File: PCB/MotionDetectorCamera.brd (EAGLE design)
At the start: 211.5 x 44.5 mm, 172 parts, among them J1 JUMPER-SOLDER, J12 JUMPER-AMPHENOL-10129380-9020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, J13 JUMPER-AMPHENOL-10129380-9020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, J14 JUMPER-AMPHENOL-10129380-9020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, J15 JUMPER-AMPHENOL-10129380-9020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, J2 JUMPER-SOLDER, J4 JUMPER-AMPHENOL-10129380-9020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, J5 JUMPER-SOLDER, J6 S-MOUNT-LENS-HOLDER, J7 MICROSD-SOCKET, J8 MINI-USB-JACK, Q10 PMOS-NEXPERIA-SOT1220, Q2 PMOS-NEXPERIA-SOT1220, Q3 PMOS-NEXPERIA-SOT1220, U1 NEXPERIA-74LVC1G98-BUFFER, U10 TI-TPS22919DCK, U11 TI-TPS2116, U12 TI-MSP430FR2422IRHL, U14 PANASONIC-EKMB110711X, U15 LATTICE-ICE40HX4K-BG121, U16 MICROCHIP-MCP7383X, U17 ON-AR0330CS1C12SPKA0, U18 ALLIANCE-AS4C8M16MSA-6BIN, U19 STM-STM32F730, U2 DIODESINC-AP7350, U20 DIODESINC-DT1446-04V-7, U21 NXP-NTB0102, U22 NXP-NTB0102, U23 TI-TPS6280XYKAR, U24 NEXPERIA-74LVC1G98-OR-INV-INP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, U28 NEXPERIA-74LVC1G98-NOR, U3 TI-TPS6280XYKAR, U30 TI-TPS22919DCK, U4 TI-TPS6280XYKAR, U5 WINBOND-W25Q40EW, U6 TI-TPS22919DCK, U7 TI-TPS22919DCK, U8 TI-TPS22919DCK, U9 TI-TPS22919DCK, X1 EPSON-FC-135, X2 SITIME-SIT8021, X3 SITIME-SIT8021

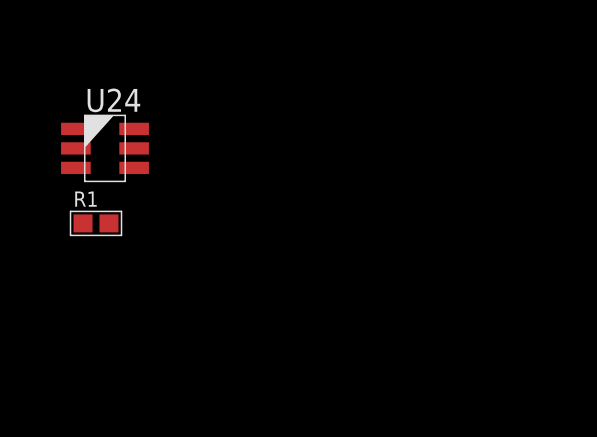
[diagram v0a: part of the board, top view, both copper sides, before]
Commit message: Add reverse current blocking diode to LDO
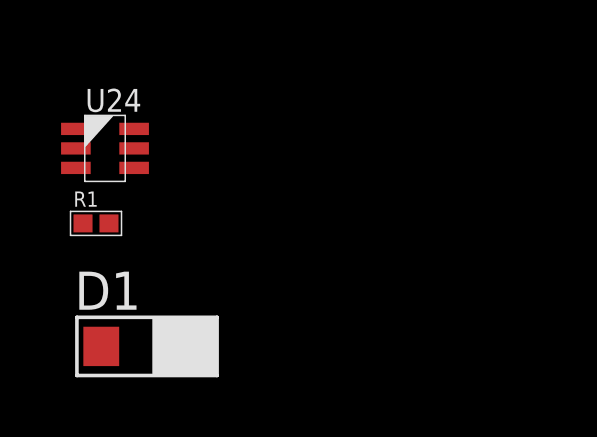
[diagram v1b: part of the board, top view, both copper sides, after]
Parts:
- added D1: ROHM-RB168MM-40, EagleLibrary:ROHM-SOD-123FL
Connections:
- net N$3: now also D1.1
- net VDD_A: now also D1.2
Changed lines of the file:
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@@
 <attribute name="PN" value="RC0402JR-0710KL" x="-14.7" y="-110.1" size="1.778" layer="27" display="off"/>
 </element>
+<element name="D1" library="EagleLibrary" package="ROHM-SOD-123FL" value="ROHM-RB168MM-40" x="-13" y="-114.2" smashed="yes">
+<attribute name="MFG" value="ROHM" x="-13" y="-114.2" size="1.778" layer="27" display="off"/>
+<attribute name="NAME" x="-15.41" y="-112.9781" size="1.27" layer="25" font="vector"/>
+<attribute name="PN" value="RB168MM-40" x="-13" y="-114.2" size="1.778" layer="27" display="off"/>
+</element>
 </elements>
 <signals>
@@
 <contactref element="Q10" pad="4"/>
 <contactref element="Q10" pad="8"/>
-<wire x1="91.1" y1="9.625" x2="92.035" y2="9.75" width="0" layer="19" extent="1-1"/>
-<wire x1="72.74" y1="5.65" x2="91.1" y2="9.625" width="0" layer="19" extent="1-1"/>
-<wire x1="71.26" y1="5.65" x2="72.74" y2="5.65" width="0" layer="19" extent="1-1"/>
+<contactref element="D1" pad="2"/>
+<wire x1="71.26" y1="5.65" x2="-11.475" y2="-114.2" width="0" layer="19" extent="1-1"/>
+<wire x1="72.74" y1="5.65" x2="71.26" y2="5.65" width="0" layer="19" extent="1-1"/>
 <wire x1="71.525" y1="8.475" x2="71.26" y2="5.65" width="0" layer="19" extent="1-1"/>
 <wire x1="71.875" y1="8.475" x2="71.525" y2="8.475" width="0" layer="19" extent="1-1"/>
+<wire x1="91.1" y1="9.625" x2="72.74" y2="5.65" width="0" layer="19" extent="1-1"/>
+<wire x1="92.035" y1="9.75" x2="91.1" y2="9.625" width="0" layer="19" extent="1-1"/>
 </signal>
 <signal name="N$42">
@@
 <contactref element="J15" pad="1"/>
 <contactref element="U2" pad="3"/>
+<contactref element="D1" pad="1"/>
+<wire x1="-14.77" y1="-76.585" x2="-14.525" y2="-114.2" width="0" layer="19" extent="1-1"/>
 <wire x1="71.875" y1="8.125" x2="-14.77" y2="-76.585" width="0" layer="19" extent="1-1"/>
 </signal>

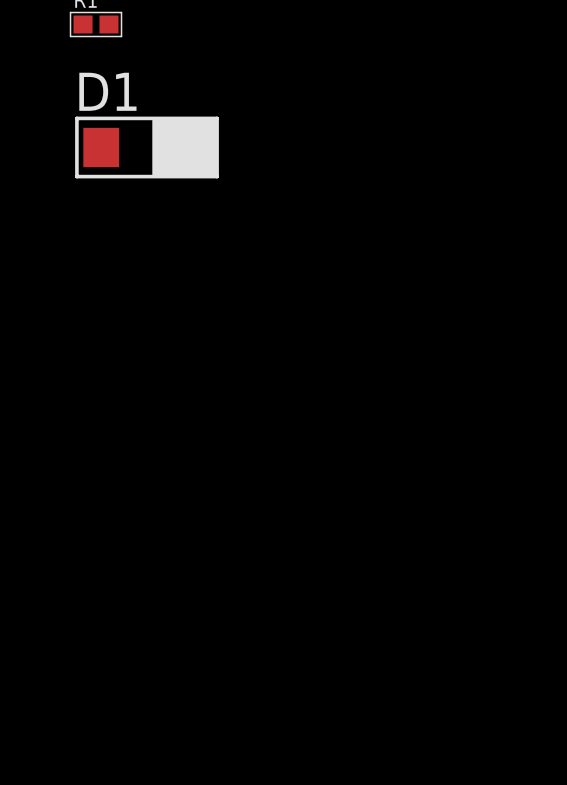
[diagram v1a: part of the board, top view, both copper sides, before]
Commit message: Working on adding bypass capacitors
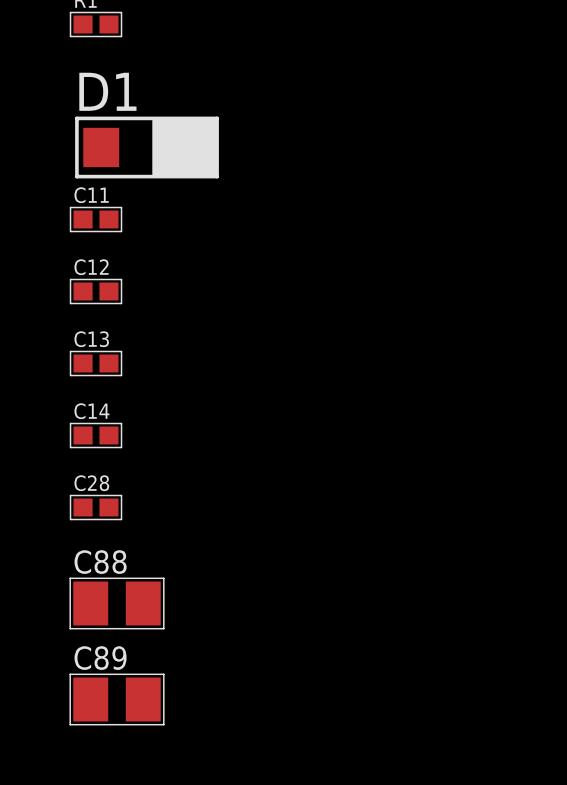
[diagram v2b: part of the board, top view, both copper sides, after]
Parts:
- added C11, C12, C13, C14, C28: 100n, EagleLibrary:0402
- added C88, C89: 10u, EagleLibrary:0805
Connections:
- net GND: now also C11.2, C12.2, C13.2, C14.2, C28.2, C88.2, C89.2
- net VDD_A_3V3: now also C11.1, C12.1
- net VDD_BAT: now also C88.1
- net VDD_B_1V8: now also C14.1, C28.1
- net VDD_B_1V8_STM: now also C13.1
- net VDD_USB: now also C89.1

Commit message: Progress
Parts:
- added C90: 10u, EagleLibrary:0805
- moved C88 6.40 mm to (-14.0, -135.8)
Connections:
- net GND: now also C90.2
- net VDD_USB: now also C90.1
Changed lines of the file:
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@@
 <attribute name="PN" value="GRM155R61H104KE19D" x="-14.7" y="-126.2" size="1.778" layer="27" display="off"/>
 </element>
-<element name="C88" library="EagleLibrary" package="0805" value="10u" x="-14" y="-129.4" smashed="yes">
-<attribute name="MFG" value="Samsung" x="-14" y="-129.4" size="1.778" layer="27" display="off"/>
-<attribute name="NAME" x="-15.469" y="-128.3993" size="0.762" layer="25" font="vector"/>
-<attribute name="PN" value="CL21A106KOQNNNE" x="-14" y="-129.4" size="1.778" layer="27" display="off"/>
-</element>
 <element name="C89" library="EagleLibrary" package="0805" value="10u" x="-14" y="-132.6" smashed="yes">
 <attribute name="MFG" value="Samsung" x="-14" y="-132.6" size="1.778" layer="27" display="off"/>
@@
 <attribute name="PN" value="CL21A106KOQNNNE" x="-14" y="-132.6" size="1.778" layer="27" display="off"/>
 </element>
+<element name="C88" library="EagleLibrary" package="0805" value="10u" x="-14" y="-135.8" smashed="yes">
+<attribute name="MFG" value="Samsung" x="-14" y="-135.8" size="1.778" layer="27" display="off"/>
+<attribute name="NAME" x="-15.469" y="-134.7993" size="0.762" layer="25" font="vector"/>
+<attribute name="PN" value="CL21A106KOQNNNE" x="-14" y="-135.8" size="1.778" layer="27" display="off"/>
+</element>
+<element name="C90" library="EagleLibrary" package="0805" value="10u" x="-14" y="-139" smashed="yes">
+<attribute name="MFG" value="Samsung" x="-14" y="-139" size="1.778" layer="27" display="off"/>
+<attribute name="NAME" x="-15.469" y="-137.9993" size="0.762" layer="25" font="vector"/>
+<attribute name="PN" value="CL21A106KOQNNNE" x="-14" y="-139" size="1.778" layer="27" display="off"/>
+</element>
 </elements>
 <signals>
@@
 <contactref element="C14" pad="2"/>
 <contactref element="C28" pad="2"/>
-<contactref element="C88" pad="2"/>
 <contactref element="C89" pad="2"/>
+<contactref element="C88" pad="2"/>
+<contactref element="C90" pad="2"/>
 <wire x1="121.9325" y1="35.3" x2="120.9377" y2="37.7" width="0" layer="19" extent="1-1"/>
 <wire x1="119.8296" y1="29.5" x2="121.9325" y2="35.3" width="0" layer="19" extent="1-1"/>
@@
 <wire x1="-14.2675" y1="-123.8" x2="-14.2675" y2="-121.4" width="0" layer="19" extent="1-1"/>
 <wire x1="-14.2675" y1="-126.2" x2="-14.2675" y2="-123.8" width="0" layer="19" extent="1-1"/>
-<wire x1="-13.1246" y1="-129.4" x2="-14.2675" y2="-126.2" width="0" layer="19" extent="1-1"/>
-<wire x1="-13.1246" y1="-132.6" x2="-13.1246" y2="-129.4" width="0" layer="19" extent="1-1"/>
+<wire x1="-13.1246" y1="-132.6" x2="-14.2675" y2="-126.2" width="0" layer="19" extent="1-1"/>
+<wire x1="-13.1246" y1="-135.8" x2="-13.1246" y2="-132.6" width="0" layer="19" extent="1-1"/>
+<wire x1="-13.1246" y1="-139" x2="-13.1246" y2="-135.8" width="0" layer="19" extent="1-1"/>
 </signal>
 <signal name="ICE_IMG_CLK16MHZ">
@@
 <contactref element="U11" pad="5"/>
 <contactref element="C89" pad="1"/>
+<contactref element="C90" pad="1"/>
+<wire x1="-14.8754" y1="-132.6" x2="-14.8754" y2="-139" width="0" layer="19" extent="1-1"/>
 <wire x1="-15.1325" y1="-82.5" x2="-14.8754" y2="-132.6" width="0" layer="19" extent="1-1"/>
 <wire x1="-12.23" y1="-64.615" x2="-15.1325" y2="-82.5" width="0" layer="19" extent="1-1"/>
@@
 <contactref element="U16" pad="3"/>
 <contactref element="C88" pad="1"/>
-<wire x1="-14.2675" y1="-39.7" x2="-14.8754" y2="-129.4" width="0" layer="19" extent="1-1"/>
+<wire x1="-14.2675" y1="-39.7" x2="-14.8754" y2="-135.8" width="0" layer="19" extent="1-1"/>
 <wire x1="-14.5" y1="-35.675" x2="-14.2675" y2="-39.7" width="0" layer="19" extent="1-1"/>
 <wire x1="-13.565" y1="-35.55" x2="-14.5" y2="-35.675" width="0" layer="19" extent="1-1"/>

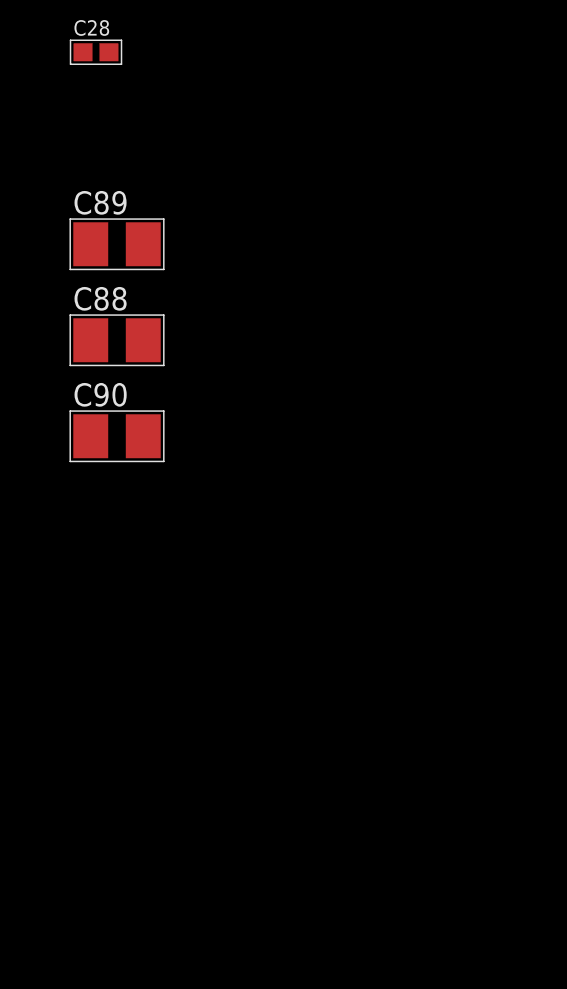
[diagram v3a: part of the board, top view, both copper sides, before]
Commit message: Added bypass caps
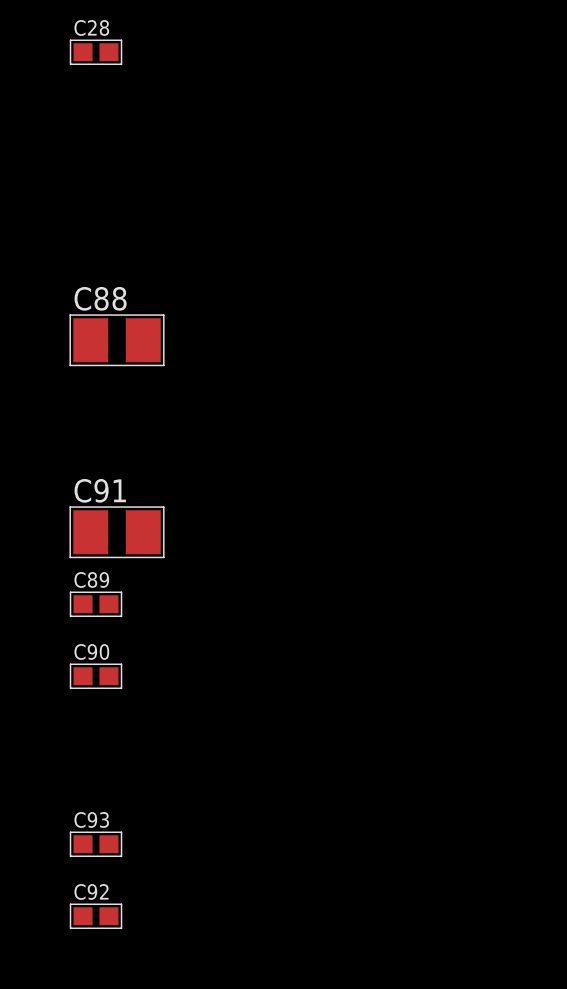
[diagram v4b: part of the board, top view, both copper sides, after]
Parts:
- added C91: 10u, EagleLibrary:0805
- added C92, C93: 100n, EagleLibrary:0402
- C89, C90: value 10u -> 2.2u; device EagleLibrary:0805 -> EagleLibrary:0402
- moved C89 12.0 mm to (-14.7, -144.6)
- moved C90 8.03 mm to (-14.7, -147.0)
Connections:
- net GND: now also C91.2, C92.2, C93.2
- net N$3: now also C92.1
- net VDD_A: now also C91.1, C93.1

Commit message: Progress
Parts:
- moved C88 22.4 mm to (-14.0, -158.2)
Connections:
- new net BAT_CHRG_STAT: U16.1
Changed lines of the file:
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@@
 <attribute name="PN" value="GRM155R61H104KE19D" x="-14.7" y="-126.2" size="1.778" layer="27" display="off"/>
 </element>
-<element name="C88" library="EagleLibrary" package="0805" value="10u" x="-14" y="-135.8" smashed="yes">
-<attribute name="MFG" value="Samsung" x="-14" y="-135.8" size="1.778" layer="27" display="off"/>
-<attribute name="NAME" x="-15.469" y="-134.7993" size="0.762" layer="25" font="vector"/>
-<attribute name="PN" value="CL21A106KOQNNNE" x="-14" y="-135.8" size="1.778" layer="27" display="off"/>
-</element>
 <element name="C91" library="EagleLibrary" package="0805" value="10u" x="-14" y="-142.2" smashed="yes">
 <attribute name="MFG" value="Samsung" x="-14" y="-142.2" size="1.778" layer="27" display="off"/>
@@
 <attribute name="PN" value="GRM155R61H104KE19D" x="-14.7" y="-155" size="1.778" layer="27" display="off"/>
 </element>
+<element name="C88" library="EagleLibrary" package="0805" value="10u" x="-14" y="-158.2" smashed="yes">
+<attribute name="MFG" value="Samsung" x="-14" y="-158.2" size="1.778" layer="27" display="off"/>
+<attribute name="NAME" x="-15.469" y="-157.1993" size="0.762" layer="25" font="vector"/>
+<attribute name="PN" value="CL21A106KOQNNNE" x="-14" y="-158.2" size="1.778" layer="27" display="off"/>
+</element>
 </elements>
 <signals>
@@
 <contactref element="C14" pad="2"/>
 <contactref element="C28" pad="2"/>
-<contactref element="C88" pad="2"/>
 <contactref element="C91" pad="2"/>
 <contactref element="C89" pad="2"/>
@@
 <contactref element="C93" pad="2"/>
 <contactref element="C92" pad="2"/>
+<contactref element="C88" pad="2"/>
+<wire x1="-14.2675" y1="-155" x2="-13.1246" y2="-158.2" width="0" layer="19" extent="1-1"/>
 <wire x1="-14.2675" y1="-152.6" x2="-14.2675" y2="-155" width="0" layer="19" extent="1-1"/>
 <wire x1="-14.2675" y1="-147" x2="-14.2675" y2="-152.6" width="0" layer="19" extent="1-1"/>
 <wire x1="-14.2675" y1="-144.6" x2="-14.2675" y2="-147" width="0" layer="19" extent="1-1"/>
 <wire x1="-13.1246" y1="-142.2" x2="-14.2675" y2="-144.6" width="0" layer="19" extent="1-1"/>
-<wire x1="-13.1246" y1="-135.8" x2="-13.1246" y2="-142.2" width="0" layer="19" extent="1-1"/>
-<wire x1="-14.2675" y1="-126.2" x2="-13.1246" y2="-135.8" width="0" layer="19" extent="1-1"/>
+<wire x1="-14.2675" y1="-126.2" x2="-13.1246" y2="-142.2" width="0" layer="19" extent="1-1"/>
 <wire x1="-14.2675" y1="-123.8" x2="-14.2675" y2="-126.2" width="0" layer="19" extent="1-1"/>
 <wire x1="-14.2675" y1="-121.4" x2="-14.2675" y2="-123.8" width="0" layer="19" extent="1-1"/>
@@
 <contactref element="U16" pad="3"/>
 <contactref element="C88" pad="1"/>
-<wire x1="-14.2675" y1="-39.7" x2="-14.8754" y2="-135.8" width="0" layer="19" extent="1-1"/>
+<wire x1="-14.2675" y1="-39.7" x2="-14.8754" y2="-158.2" width="0" layer="19" extent="1-1"/>
 <wire x1="-14.5" y1="-35.675" x2="-14.2675" y2="-39.7" width="0" layer="19" extent="1-1"/>
 <wire x1="-13.565" y1="-35.55" x2="-14.5" y2="-35.675" width="0" layer="19" extent="1-1"/>
@@
 <wire x1="-15.0346" y1="-99.95" x2="-13.4296" y2="-108.25" width="0" layer="19" extent="1-1"/>
 </signal>
+<signal name="BAT_CHRG_STAT">
+<contactref element="U16" pad="1"/>
+</signal>
 </signals>

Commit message: Progress
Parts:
- added Q1: PMOS-NEXPERIA-SOT1220, EagleLibrary:NEXPERIA-SOT1220
- added R35: 100k, EagleLibrary:0402
- R5, R6: value 100k -> 300k
- moved R7 116.5 mm to (-14.9, -171.1)
- moved R6 116.5 mm to (-14.9, -168.7)
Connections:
- removed net N$36: R5.2, R6.1
- removed net N$39: R6.2, R7.1
- new net BAT_CHRG_LVL: R35.1, R6.2
- new net BAT_CHRG_LVL_EN_: Q1.3, R7.2
- new net N$46: Q1.1, Q1.2, Q1.5, Q1.6, Q1.7, R6.1
- net GND: now also R35.2
- net N$42: now also R5.2; no longer R7.2
- net VDD_BAT: now also Q1.4, Q1.8, R7.1
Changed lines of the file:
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@@
 <attribute name="PN" value="10129380-902002ALF" x="-20.2" y="-37.8" size="1.778" layer="27" display="off"/>
 </element>
-<element name="R5" library="EagleLibrary" package="0402" value="100k" x="-14.7" y="-49.8" smashed="yes">
-<attribute name="MFG" value="Stackpole" x="-14.7" y="-49.8" size="1.778" layer="27" display="off"/>
+<element name="R5" library="EagleLibrary" package="0402" value="300k" x="-14.7" y="-49.8" smashed="yes">
 <attribute name="NAME" x="-15.454" y="-49.244" size="0.508" layer="25" font="vector"/>
-<attribute name="PN" value="RMCF0402JT100K" x="-14.7" y="-49.8" size="1.778" layer="27" display="off"/>
-</element>
-<element name="R6" library="EagleLibrary" package="0402" value="100k" x="-14.7" y="-52.2" smashed="yes">
-<attribute name="MFG" value="Stackpole" x="-14.7" y="-52.2" size="1.778" layer="27" display="off"/>
-<attribute name="NAME" x="-15.454" y="-51.644" size="0.508" layer="25" font="vector"/>
-<attribute name="PN" value="RMCF0402JT100K" x="-14.7" y="-52.2" size="1.778" layer="27" display="off"/>
-</element>
-<element name="R7" library="EagleLibrary" package="0402" value="100k" x="-14.7" y="-54.6" smashed="yes">
-<attribute name="MFG" value="Stackpole" x="-14.7" y="-54.6" size="1.778" layer="27" display="off"/>
-<attribute name="NAME" x="-15.454" y="-54.044" size="0.508" layer="25" font="vector"/>
-<attribute name="PN" value="RMCF0402JT100K" x="-14.7" y="-54.6" size="1.778" layer="27" display="off"/>
 </element>
 <element name="R8" library="EagleLibrary" package="0402" value="100k" x="-14.7" y="-57" smashed="yes">
@@
 <attribute name="PN" value="CL21A106KOQNNNE" x="-14" y="-158.2" size="1.778" layer="27" display="off"/>
 </element>
+<element name="R35" library="EagleLibrary" package="0402" value="100k" x="-12.6" y="-163" smashed="yes">
+<attribute name="MFG" value="Stackpole" x="-14.9" y="-167.8" size="1.778" layer="27" display="off"/>
+<attribute name="NAME" x="-13.354" y="-162.444" size="0.508" layer="25" font="vector"/>
+<attribute name="PN" value="RMCF0402JT100K" x="-14.9" y="-167.8" size="1.778" layer="27" display="off"/>
+</element>
+<element name="Q1" library="EagleLibrary" package="NEXPERIA-SOT1220" value="PMOS-NEXPERIA-SOT1220" x="-14.7" y="-166.3" smashed="yes">
+<attribute name="MFG" value="Nexperia" x="-14.7" y="-166.3" size="1.778" layer="27" display="off"/>
+<attribute name="NAME" x="-15.652" y="-165.2056" size="0.762" layer="25" font="vector"/>
+<attribute name="PN" value="PMPB10UPX" x="-14.7" y="-166.3" size="1.778" layer="27" display="off"/>
+</element>
+<element name="R6" library="EagleLibrary" package="0402" value="300k" x="-14.9" y="-168.7" smashed="yes">
+<attribute name="NAME" x="-15.654" y="-168.144" size="0.508" layer="25" font="vector"/>
+</element>
+<element name="R7" library="EagleLibrary" package="0402" value="100k" x="-14.9" y="-171.1" smashed="yes">
+<attribute name="MFG" value="Stackpole" x="-14.9" y="-171.1" size="1.778" layer="27" display="off"/>
+<attribute name="NAME" x="-15.654" y="-170.544" size="0.508" layer="25" font="vector"/>
+<attribute name="PN" value="RMCF0402JT100K" x="-14.9" y="-171.1" size="1.778" layer="27" display="off"/>
+</element>
 </elements>
 <signals>
@@
 <contactref element="C92" pad="2"/>
 <contactref element="C88" pad="2"/>
+<contactref element="R35" pad="2"/>
+<wire x1="-13.1246" y1="-158.2" x2="-12.1675" y2="-163" width="0" layer="19" extent="1-1"/>
 <wire x1="-14.2675" y1="-155" x2="-13.1246" y2="-158.2" width="0" layer="19" extent="1-1"/>
 <wire x1="-14.2675" y1="-152.6" x2="-14.2675" y2="-155" width="0" layer="19" extent="1-1"/>
@@
 <contactref element="U16" pad="3"/>
 <contactref element="C88" pad="1"/>
+<contactref element="Q1" pad="4"/>
+<contactref element="Q1" pad="8"/>
+<contactref element="R7" pad="1"/>
+<wire x1="-14.7" y1="-167.075" x2="-15.3325" y2="-171.1" width="0" layer="19" extent="1-1"/>
+<wire x1="-13.765" y1="-166.95" x2="-14.7" y2="-167.075" width="0" layer="19" extent="1-1"/>
+<wire x1="-14.8754" y1="-158.2" x2="-13.765" y2="-166.95" width="0" layer="19" extent="1-1"/>
 <wire x1="-14.2675" y1="-39.7" x2="-14.8754" y2="-158.2" width="0" layer="19" extent="1-1"/>
 <wire x1="-14.5" y1="-35.675" x2="-14.2675" y2="-39.7" width="0" layer="19" extent="1-1"/>
@@
 <signal name="N$42">
 <contactref element="U11" pad="4"/>
-<contactref element="R7" pad="2"/>
 <contactref element="R8" pad="1"/>
-<wire x1="-14.2675" y1="-54.6" x2="71.26" y2="4.65" width="0" layer="19" extent="1-1"/>
-<wire x1="-15.1325" y1="-57" x2="-14.2675" y2="-54.6" width="0" layer="19" extent="1-1"/>
+<contactref element="R5" pad="2"/>
+<wire x1="-14.2675" y1="-49.8" x2="71.26" y2="4.65" width="0" layer="19" extent="1-1"/>
+<wire x1="-15.1325" y1="-57" x2="-14.2675" y2="-49.8" width="0" layer="19" extent="1-1"/>
 </signal>
 <signal name="N$21">
@@
 <wire x1="-15.435" y1="-32.25" x2="-15.435" y2="-34.25" width="0" layer="19" extent="1-1"/>
 </signal>
-<signal name="N$36">
-<contactref element="R5" pad="2"/>
-<contactref element="R6" pad="1"/>
-<wire x1="-14.2675" y1="-49.8" x2="-15.1325" y2="-52.2" width="0" layer="19" extent="1-1"/>
-</signal>
-<signal name="N$39">
-<contactref element="R6" pad="2"/>
-<contactref element="R7" pad="1"/>
-<wire x1="-14.2675" y1="-52.2" x2="-15.1325" y2="-54.6" width="0" layer="19" extent="1-1"/>
-</signal>
 <signal name="N$3">
 <contactref element="J15" pad="1"/>
@@
 <contactref element="U16" pad="1"/>
 </signal>
+<signal name="BAT_CHRG_LVL">
+<contactref element="R35" pad="1"/>
+<contactref element="R6" pad="2"/>
+<wire x1="-13.0325" y1="-163" x2="-14.4675" y2="-168.7" width="0" layer="19" extent="1-1"/>
+</signal>
+<signal name="N$46">
+<contactref element="Q1" pad="2" route="any" routetag="G$1.D"/>
+<contactref element="Q1" pad="7" route="any" routetag="G$1.D"/>
+<contactref element="Q1" pad="5" route="any" routetag="G$1.D"/>
+<contactref element="Q1" pad="1" route="any" routetag="G$1.D"/>
+<contactref element="Q1" pad="6" route="any" routetag="G$1.D"/>
+<contactref element="R6" pad="1"/>
+<wire x1="-15.635" y1="-166.3" x2="-15.3325" y2="-168.7" width="0" layer="19" extent="1-1"/>
+</signal>
+<signal name="BAT_CHRG_LVL_EN_">
+<contactref element="Q1" pad="3"/>
+<contactref element="R7" pad="2"/>
+<wire x1="-15.635" y1="-166.95" x2="-14.4675" y2="-171.1" width="0" layer="19" extent="1-1"/>
+</signal>
 </signals>
